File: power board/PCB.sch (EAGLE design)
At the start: 74 parts, among them IC1 MCP2515-E/ST, Q1 BUZ10, Q2 QUARZ5, U1 INA209_PW_16, U2 UCC2837_D_8, U3 AD5252BRU10, U5 MSP430FR5739_DA_38, U6 SN65HVD235_D_8

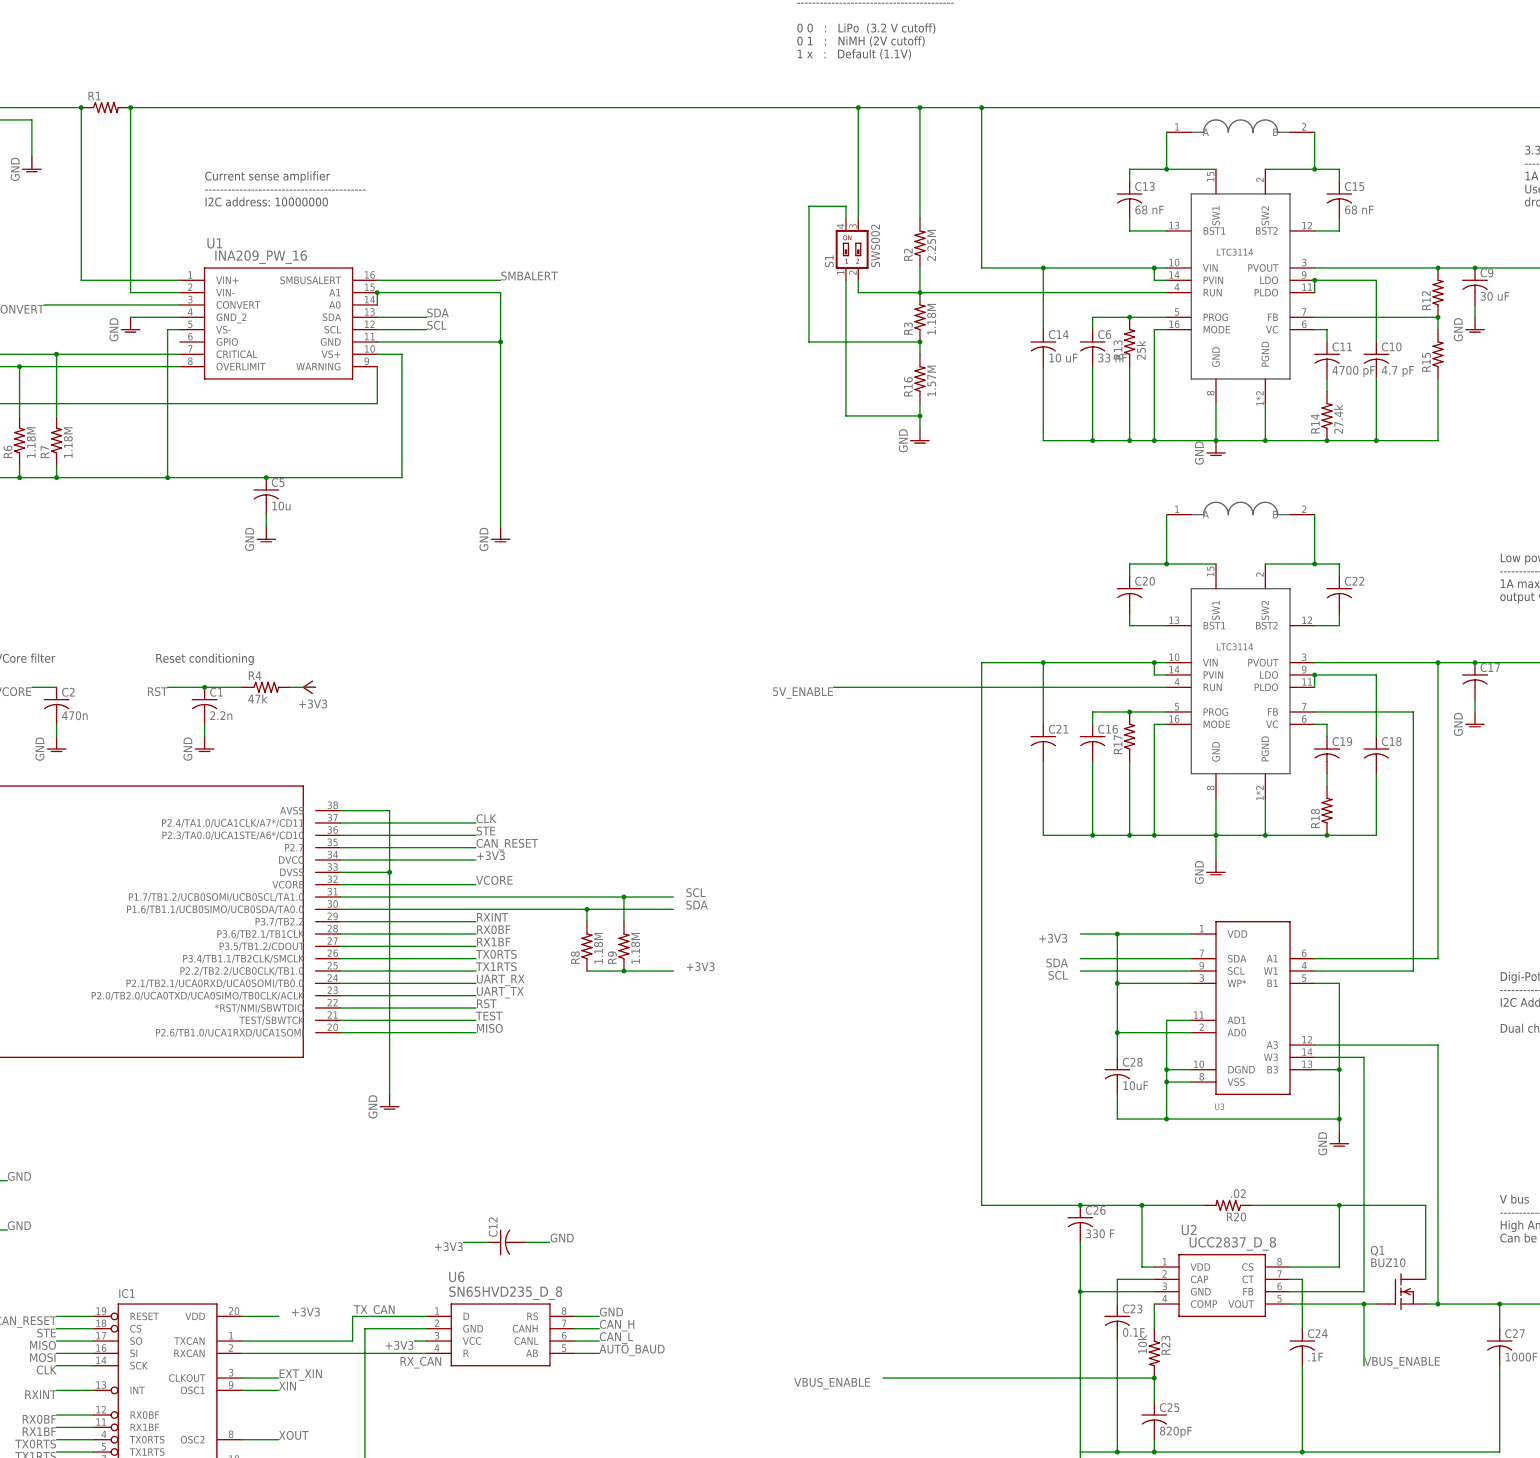
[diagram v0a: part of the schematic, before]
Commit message: PCB layout of power rails
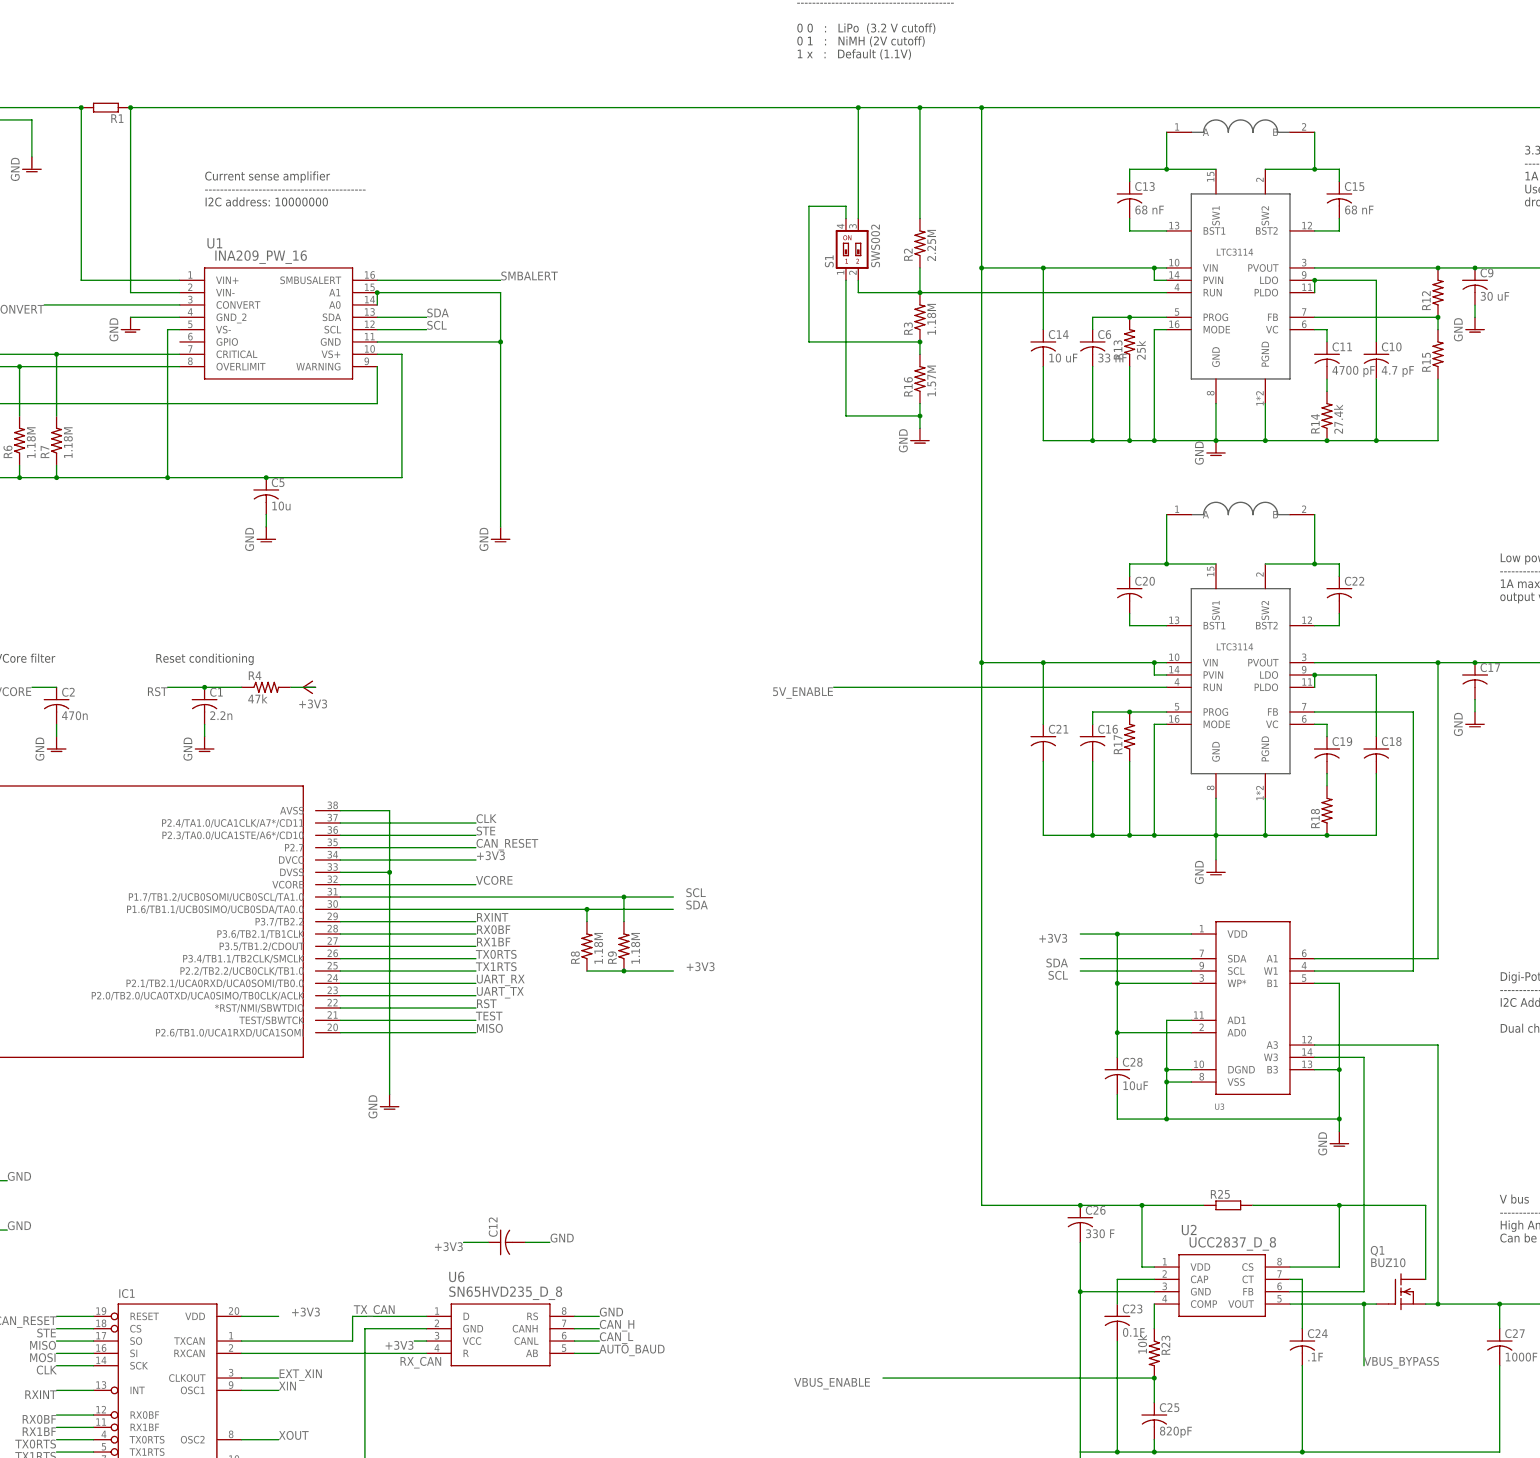
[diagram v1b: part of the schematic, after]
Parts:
- removed R20: .02, adafruit:R-US_M0805
- added R25: (no value), resistor-shunt:SMR
- R1: device resistor:R-US_R2512 -> resistor-shunt:SMR
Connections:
- removed net N$36: C21.1, C26.1, R20.2, U$3.PVIN, U$3.VIN, U2.VDD
- net BAT_WARN: now also R5.2
- net GND: now also C10.2, C14.2, C16.2, C18.2, C21.2, C23.2, C24.2, C25.2, C26.2, C27.2, C28.2, C5.2, C6.2, IC1.VSS, JP1.1, R13.1, R14.1, R15.1, R16.1, R17.1, R18.1, S1.1, U$1.GND, U$1.MODE, U$1.PGND, U$3.GND, U$3.MODE, U$3.PGND, U1.GND_2, U2.GND, U3.AD1, U3.B1, U3.B3, U3.DGND, U3.VSS, U5.AVSS_2, U6.GND
- net GNDA: no longer C10.2, C14.2, C16.2, C18.2, C21.2, C23.2, C24.2, C25.2, C26.2, C27.2, C28.2, C5.2, C6.2, IC1.VSS, JP1.1, R13.1, R14.1, R15.1, R16.1, R17.1, R18.1, S1.1, U$1.GND, U$1.MODE, U$1.PGND, U$3.GND, U$3.MODE, U$3.PGND, U1.GND_2, U2.GND, U3.AD1, U3.B1, U3.B3, U3.DGND, U3.VSS, U5.AVSS_2, U6.GND
- net N$25: now also R25.1; no longer R20.1
- net VBUS_BYPASS: now also Q1.G, U2.VOUT
- net VBUS_ENABLE: no longer Q1.G, U2.VOUT
- net VCC: now also C21.1, C26.1, R25.2, U$3.PVIN, U$3.VIN, U2.VDD

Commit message: additional pcb work
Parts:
- removed JP1: (no value), jumper:JP1E
- added U$6: MOLEX_15-31-1026, connectors:MOLEX_15-31-1026
- added X1: (no value), con-wago-500:W237-102
- JP4: device adafruit:PINHD-2X9-BIG -> con-lsta:FE05-2
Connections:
- net GND: now also C17.2, U$6.2, X1-2.KL; no longer JP1.1, JP4.12, JP4.14, JP4.16, JP4.18
- net GNDA: no longer C17.2
- net VBUS: now also U$6.1; no longer JP4.11, JP4.13, JP4.15, JP4.17
- net VCC_1: now also X1-1.KL; no longer JP1.2
- net XIN: now also C7.1, Q2.2; no longer C8.1, Q2.1
- net XOUT: now also C8.1, Q2.1; no longer C7.1, Q2.2
